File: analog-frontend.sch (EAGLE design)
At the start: 69 parts, among them IC1 ADG731, IC2 TPS63031, IC3 INA332, IC4 OPA2320, IC5 TM4C123G, IC6 NRF24L01SMD, Y1 CRYSTAL3X2, Y2 CRYSTAL3X2

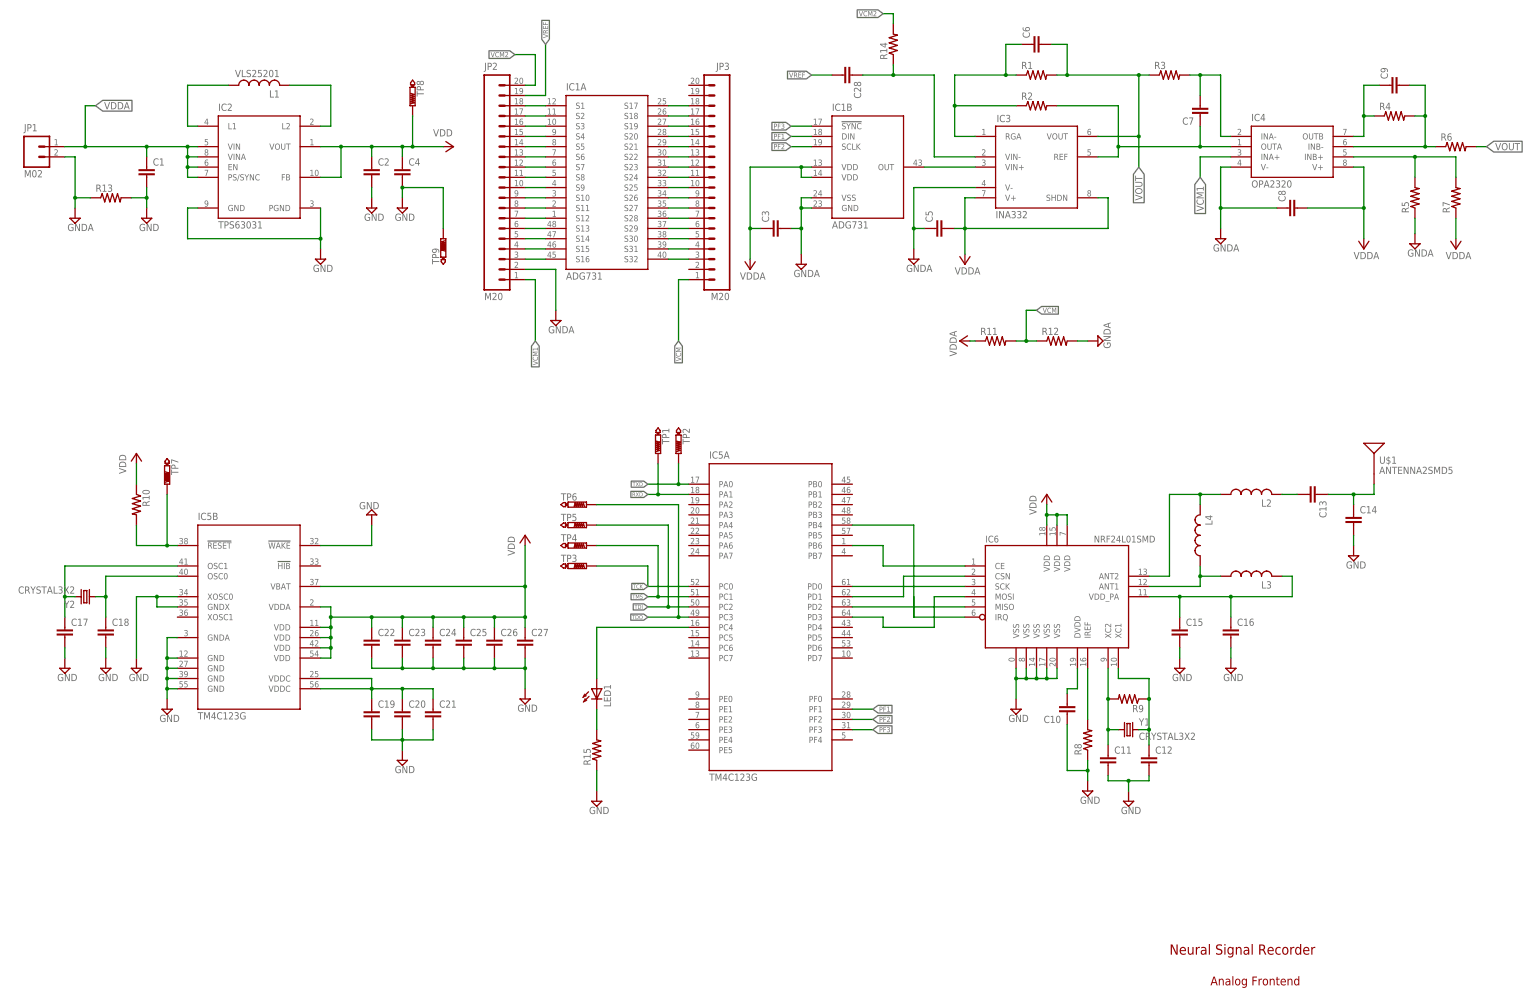
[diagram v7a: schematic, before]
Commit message: changed all components to 0402
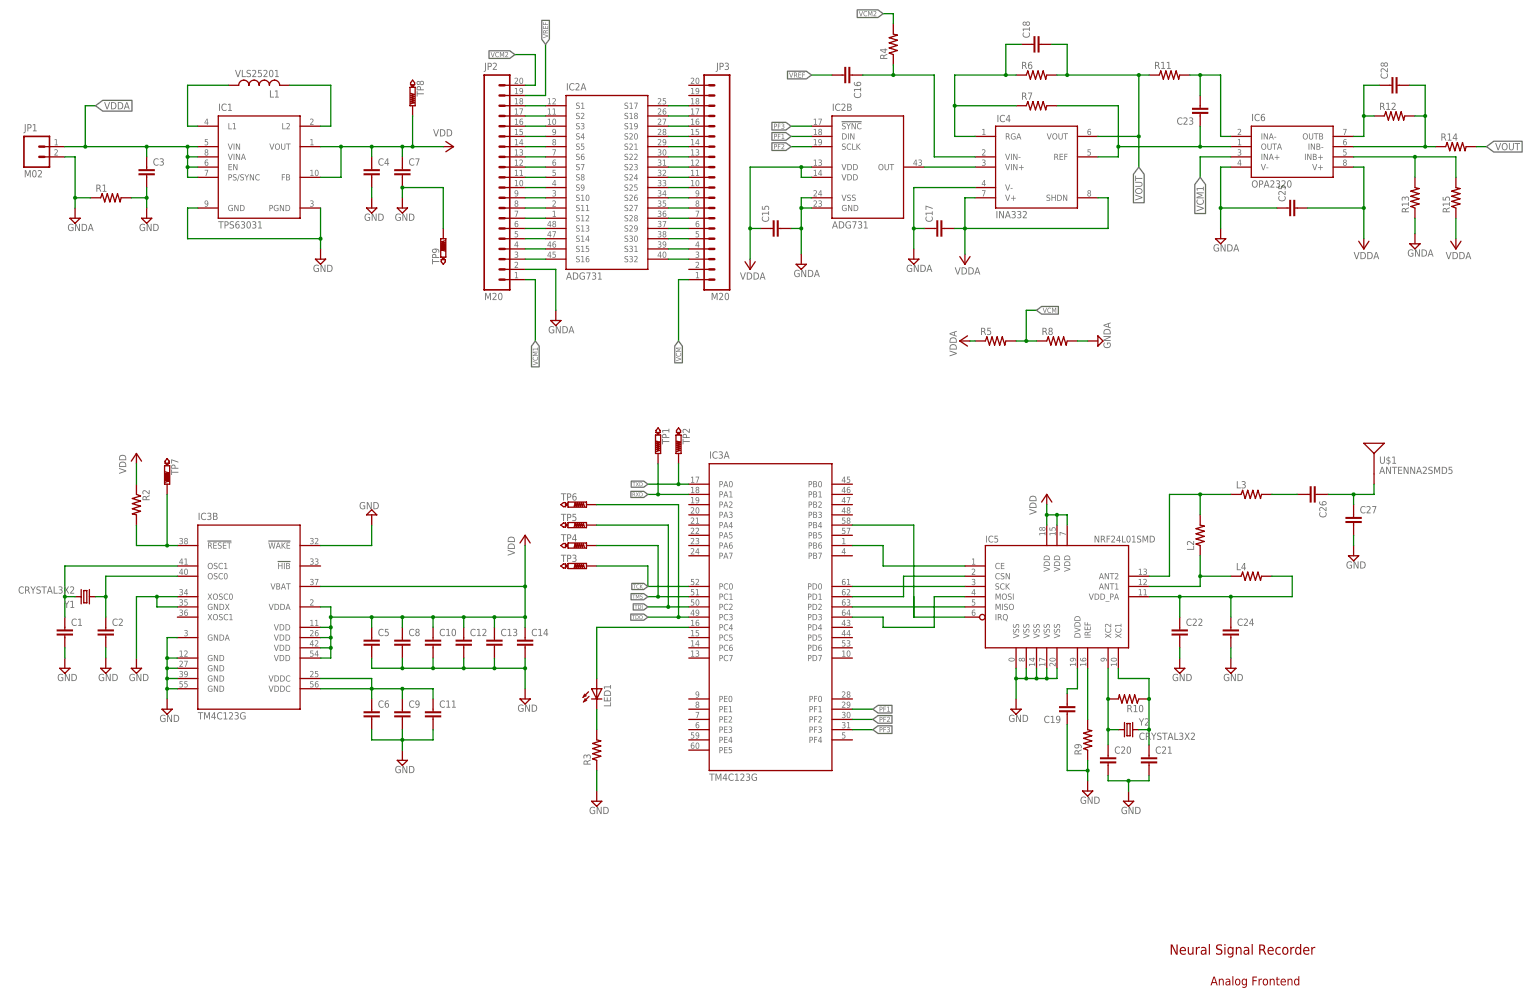
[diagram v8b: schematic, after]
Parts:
- C1, C10, C11, C12, C13, C14, C15, C16, C17, C18, C19, C2, C20, C22, C23, C24, C25, C26, C27, C28, C3, C5, C6, C8, C9: device rcl:C-EUC0201 -> rcl:C-EUC0402
- IC1: value ADG731 -> TPS63031; device mor307:ADG731 -> mor307:TPS63031
- IC2: value TPS63031 -> ADG731; device mor307:TPS63031 -> mor307:ADG731
- IC3: value INA332 -> TM4C123G; device mor307:INA332 -> mor307:TM4C123G
- IC4: value OPA2320 -> INA332; device mor307:OPA2320 -> mor307:INA332
- IC5: value TM4C123G -> NRF24L01SMD; device mor307:TM4C123G -> SparkFun-RF:NRF24L01SMD
- IC6: value NRF24L01SMD -> OPA2320; device SparkFun-RF:NRF24L01SMD -> mor307:OPA2320
- L2, L3, L4: device rcl:L-USL0201 -> rcl:R-US_R0402
- R10, R11, R12, R13, R14, R15, R2, R3, R4, R5, R6, R7, R8, R9: device rcl:R-US_R0201 -> rcl:R-US_R0402
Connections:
- net +3V3: now also C10.1, C12.1, C13.1, C14.1, C5.1, C7.1, C8.1, IC1.FB, IC1.VOUT, IC3B.VBAT, IC3B.VDD@1, IC3B.VDD@2, IC3B.VDD@3, IC3B.VDD@4, IC3B.VDDA, IC5.VDD@15, IC5.VDD@18, IC5.VDD@7, R2.1; no longer C2.1, C22.1, C23.1, C24.1, C25.1, C26.1, C27.1, IC2.FB, IC2.VOUT, IC5B.VBAT, IC5B.VDD@1, IC5B.VDD@2, IC5B.VDD@3, IC5B.VDD@4, IC5B.VDDA, IC6.VDD@15, IC6.VDD@18, IC6.VDD@7, R10.1
- net GND: now also C10.2, C13.2, C19.1, C3.2, C5.2, C6.2, C7.2, C8.2, C9.2, IC1.GND, IC1.PGND, IC3B.!WAKE!, IC3B.GND@1, IC3B.GND@2, IC3B.GND@3, IC3B.GND@4, IC3B.GNDA, IC3B.GNDX, IC3B.XOSC0, IC5.VSS@0, IC5.VSS@14, IC5.VSS@17, IC5.VSS@20, IC5.VSS@8, R1.2, R3.1, R9.1; no longer C10.1, C15.2, C16.2, C17.2, C18.2, C19.2, C23.2, C25.2, C26.2, IC2.GND, IC2.PGND, IC5B.!WAKE!, IC5B.GND@1, IC5B.GND@2, IC5B.GND@3, IC5B.GND@4, IC5B.GNDA, IC5B.GNDX, IC5B.XOSC0, IC6.VSS@0, IC6.VSS@14, IC6.VSS@17, IC6.VSS@20, IC6.VSS@8, R13.2, R15.1, R8.1
- net GNDA: now also C15.2, C17.1, C25.1, IC2B.GND, IC2B.VSS, IC6.V-, R1.1, R8.2; no longer C3.2, C5.1, C8.1, IC1B.GND, IC1B.VSS, IC3.V-, R12.2, R5.1
- net N$1: now also IC2A.S1; no longer IC1A.S1
- net N$10: now also IC2A.S7; no longer IC1A.S7
- net N$11: now also IC2A.S8; no longer IC1A.S8
- net N$12: now also IC2A.S9; no longer IC1A.S9
- net N$13: now also IC2A.S10; no longer IC1A.S10
- net N$14: now also IC2A.S11; no longer IC1A.S11
- net N$15: now also IC2A.S12; no longer IC1A.S12
- net N$16: now also IC2A.S13; no longer IC1A.S13
- net N$17: now also IC2A.S14; no longer IC1A.S14
- net N$18: now also IC2A.S15; no longer IC1A.S15
- net N$19: now also IC2A.S18; no longer IC1A.S18
- net N$2: now also IC2A.S16; no longer IC1A.S16
- net N$20: now also IC2A.S19; no longer IC1A.S19
- net N$21: now also IC2A.S20; no longer IC1A.S20
- net N$22: now also IC2A.S21; no longer IC1A.S21
- net N$23: now also IC2A.S22; no longer IC1A.S22
- net N$24: now also IC2A.S23; no longer IC1A.S23
- net N$25: now also IC2A.S24; no longer IC1A.S24
- net N$26: now also IC2A.S25; no longer IC1A.S25
- net N$27: now also IC2A.S26; no longer IC1A.S26
- net N$28: now also IC2A.S27; no longer IC1A.S27
- net N$29: now also IC2A.S28; no longer IC1A.S28
- net N$3: now also IC2A.S17; no longer IC1A.S17
- net N$30: now also IC2A.S29; no longer IC1A.S29
- net N$31: now also IC2A.S30; no longer IC1A.S30
- net N$32: now also IC2A.S31; no longer IC1A.S31
- net N$33: now also IC1.L1; no longer IC2.L1
- net N$34: now also IC1.L2; no longer IC2.L2
- net N$35: now also IC2B.OUT, IC4.VIN+; no longer IC1B.OUT, IC3.VIN+
- net N$36: now also C23.1, IC4.REF, IC6.OUTA, R7.2; no longer C7.1, IC3.REF, IC4.OUTA, R2.2
- net N$37: now also C2.1, IC3B.OSC0, Y1.1; no longer C18.1, IC5B.OSC0, Y2.1
- net N$38: now also C18.1, IC4.RGA, R6.1, R7.1; no longer C6.1, IC3.RGA, R1.1, R2.1
- net N$39: now also C28.2, IC6.INB-, R12.2, R14.1; no longer C9.2, IC4.INB-, R4.2, R6.1
- net N$4: now also IC2A.S32; no longer IC1A.S32
- net N$40: now also C1.1, IC3B.OSC1, Y1.2; no longer C17.1, IC5B.OSC1, Y2.2
- net N$41: now also C28.1, IC6.OUTB, R12.1; no longer C9.1, IC4.OUTB, R4.1
- net N$42: now also C23.2, IC6.INA-, R11.2; no longer C7.2, IC4.INA-, R3.2
- net N$43: now also C19.2, IC5.DVDD; no longer C10.2, IC6.DVDD
- net N$44: now also IC5.IREF, R9.2; no longer IC6.IREF, R8.2
- net N$45: now also C11.1, C6.1, C9.1, IC3B.VDDC@1, IC3B.VDDC@2; no longer C19.1, C20.1, C21.1, IC5B.VDDC@1, IC5B.VDDC@2
- net N$46: now also C20.1, IC5.XC2, R10.2, Y2.1; no longer C11.1, IC6.XC2, R9.2, Y1.1
- net N$47: now also IC6.INB+, R13.2, R15.2; no longer IC4.INB+, R5.2, R7.2
- net N$48: now also C21.1, IC5.XC1, R10.1, Y2.2; no longer C12.1, IC6.XC1, R9.1, Y1.2
- net N$49: now also IC3B.!RESET!, R2.2; no longer IC5B.!RESET!, R10.2
- net N$5: now also IC2A.S2; no longer IC1A.S2
- net N$50: now also IC5.ANT1, L2.1; no longer IC6.ANT1, L3.1
- net N$51: now also IC5.ANT2, L2.2, L3.1; no longer IC6.ANT2, L2.1, L4.2
- net N$52: now also C22.1, C24.1, IC5.VDD_PA, L4.2; no longer C15.1, C16.1, IC6.VDD_PA, L3.2
- net N$53: now also C26.2, L3.2; no longer C13.2, L2.2
- net N$54: now also C26.1, C27.1; no longer C13.1, C14.1
- net N$55: now also IC3A.PD0, IC5.SCK; no longer IC5A.PD0, IC6.SCK
- net N$56: now also IC3A.PD1, IC5.CSN; no longer IC5A.PD1, IC6.CSN
- net N$58: now also IC3A.PD2, IC5.MISO; no longer IC5A.PD2, IC6.MISO
- net N$59: now also IC3A.PB6, IC5.CE; no longer IC5A.PB6, IC6.CE
- net N$6: now also IC2A.S3; no longer IC1A.S3
- net N$60: now also IC3A.PB4, IC5.IRQ; no longer IC5A.PB4, IC6.IRQ
- net N$61: now also IC3A.PD3, IC5.MOSI; no longer IC5A.PD3, IC6.MOSI
- net N$62: now also C16.1, IC4.VIN-, R4.1; no longer C28.1, IC3.VIN-, R14.1
- net N$63: now also IC3A.PC4; no longer IC5A.PC4
- net N$66: now also R3.2; no longer R15.2
- net N$7: now also IC2A.S4; no longer IC1A.S4
- net N$8: now also IC2A.S5; no longer IC1A.S5
- net N$9: now also IC2A.S6; no longer IC1A.S6
- net PF1: now also IC2B.DIN, IC3A.PF1; no longer IC1B.DIN, IC5A.PF1
- net PF2: now also IC2B.SCLK, IC3A.PF2; no longer IC1B.SCLK, IC5A.PF2
- net PF3: now also IC2B.!SYNC!, IC3A.PF3; no longer IC1B.!SYNC!, IC5A.PF3
- net RXD: now also IC3A.PA1; no longer IC5A.PA1
- net TCK: now also IC3A.PC0; no longer IC5A.PC0
- net TDI: now also IC3A.PC2; no longer IC5A.PC2
- net TDO: now also IC3A.PC3; no longer IC5A.PC3
- net TMS: now also IC3A.PC1; no longer IC5A.PC1
- net TXD: now also IC3A.PA0; no longer IC5A.PA0
- net VCM: now also R5.2, R8.1; no longer R11.2, R12.1
- net VCM1: now also IC6.INA+; no longer IC4.INA+
- net VCM2: now also R4.2; no longer R14.2
- net VDDA: now also C15.1, C17.2, C25.2, IC1.EN, IC1.PS/SYNC, IC1.VIN, IC1.VINA, IC2B.VDD@1, IC2B.VDD@2, IC4.SHDN, IC6.V+, R15.1, R5.1; no longer C1.1, C5.2, C8.2, IC1B.VDD@1, IC1B.VDD@2, IC2.EN, IC2.PS/SYNC, IC2.VIN, IC2.VINA, IC3.SHDN, IC3.V+, R11.1, R7.1
- net VOUT: now also C18.2, IC4.VOUT, R11.1, R14.2; no longer C6.2, IC3.VOUT, R1.2, R3.1
- net VREF: now also C16.2; no longer C28.2
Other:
- moved on the sheet: C1, C10, C11, C12, C13, C14, C15, C16, C17, C18, C19, C2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
